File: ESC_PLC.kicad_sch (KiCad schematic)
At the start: 2 parts, among them U2 STM32WBA55HGFx

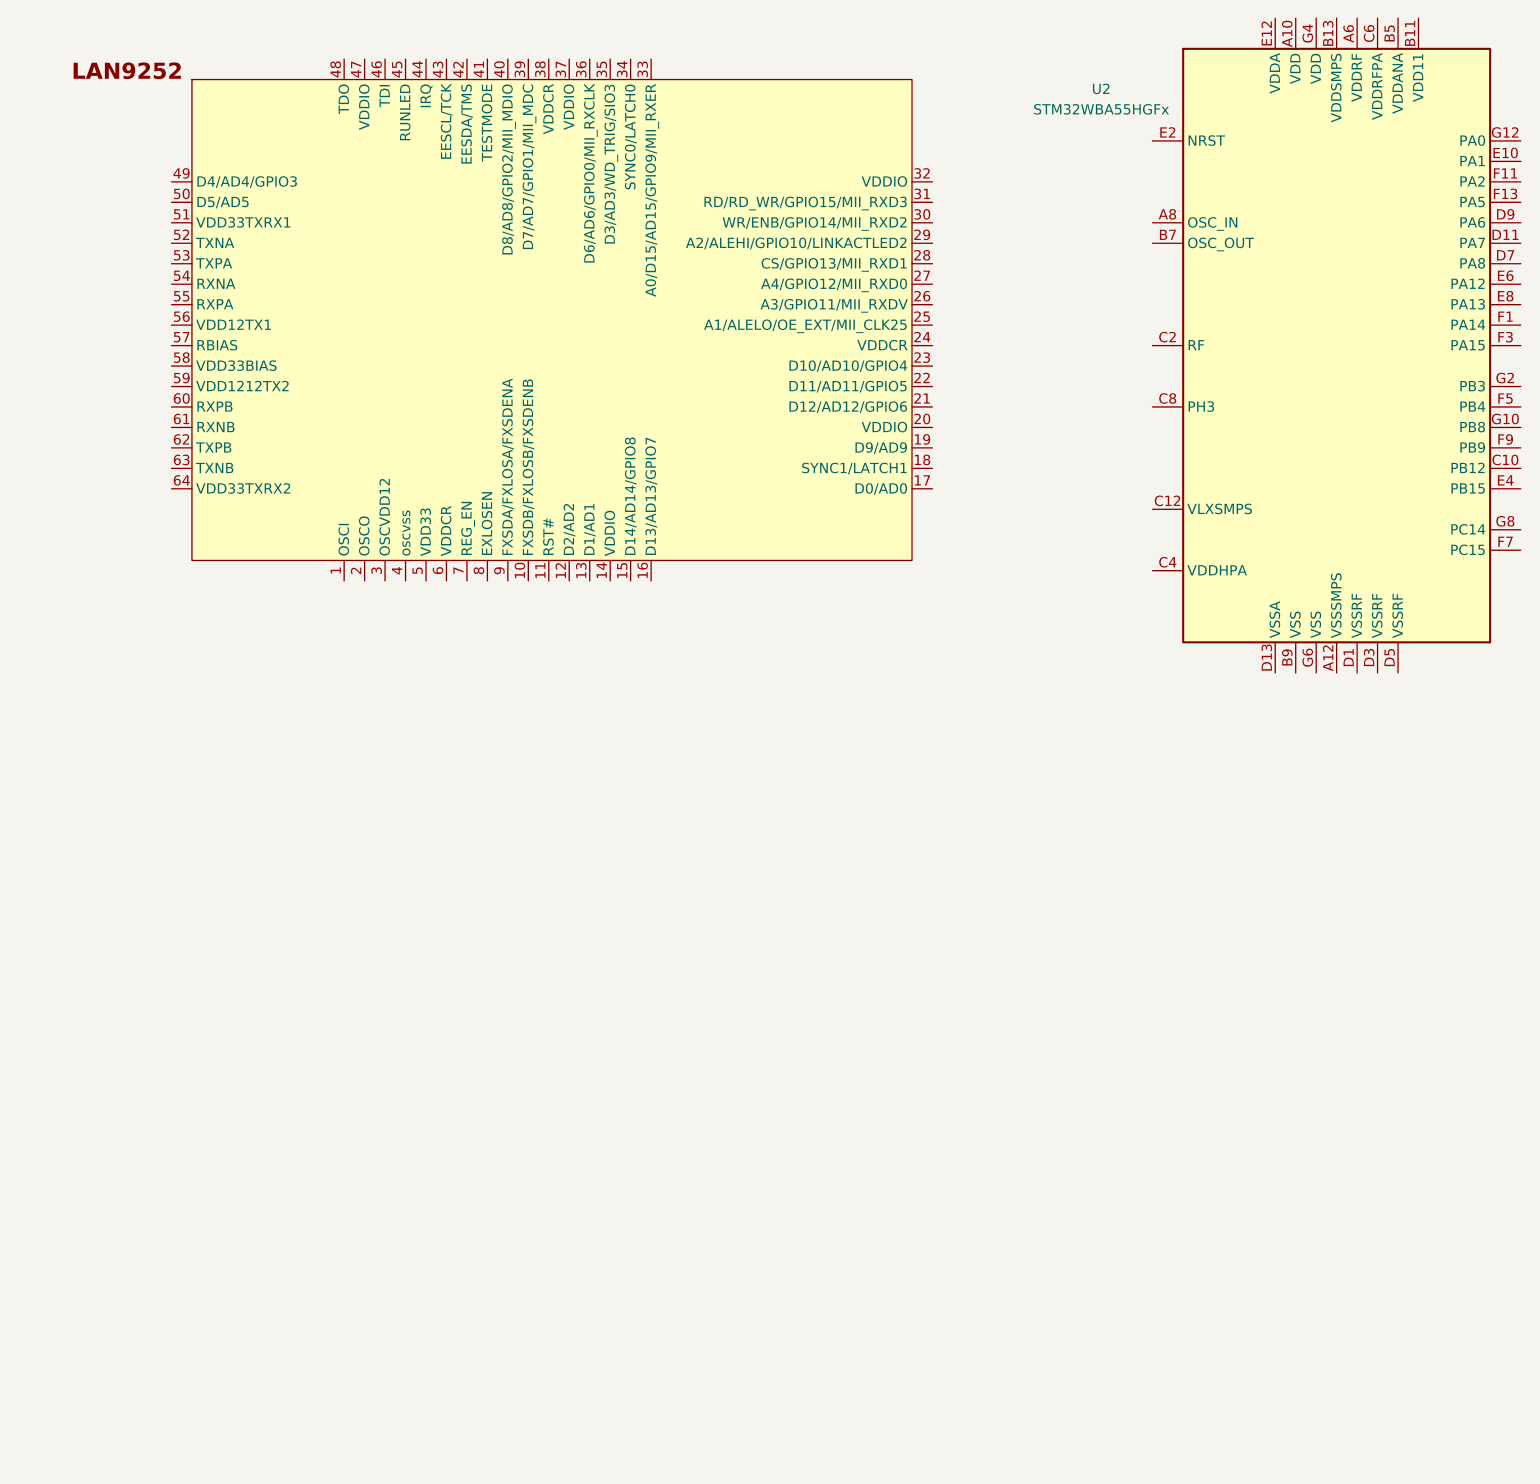
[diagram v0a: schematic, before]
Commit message: Kicad project met ethercat en al paar custom symbolen
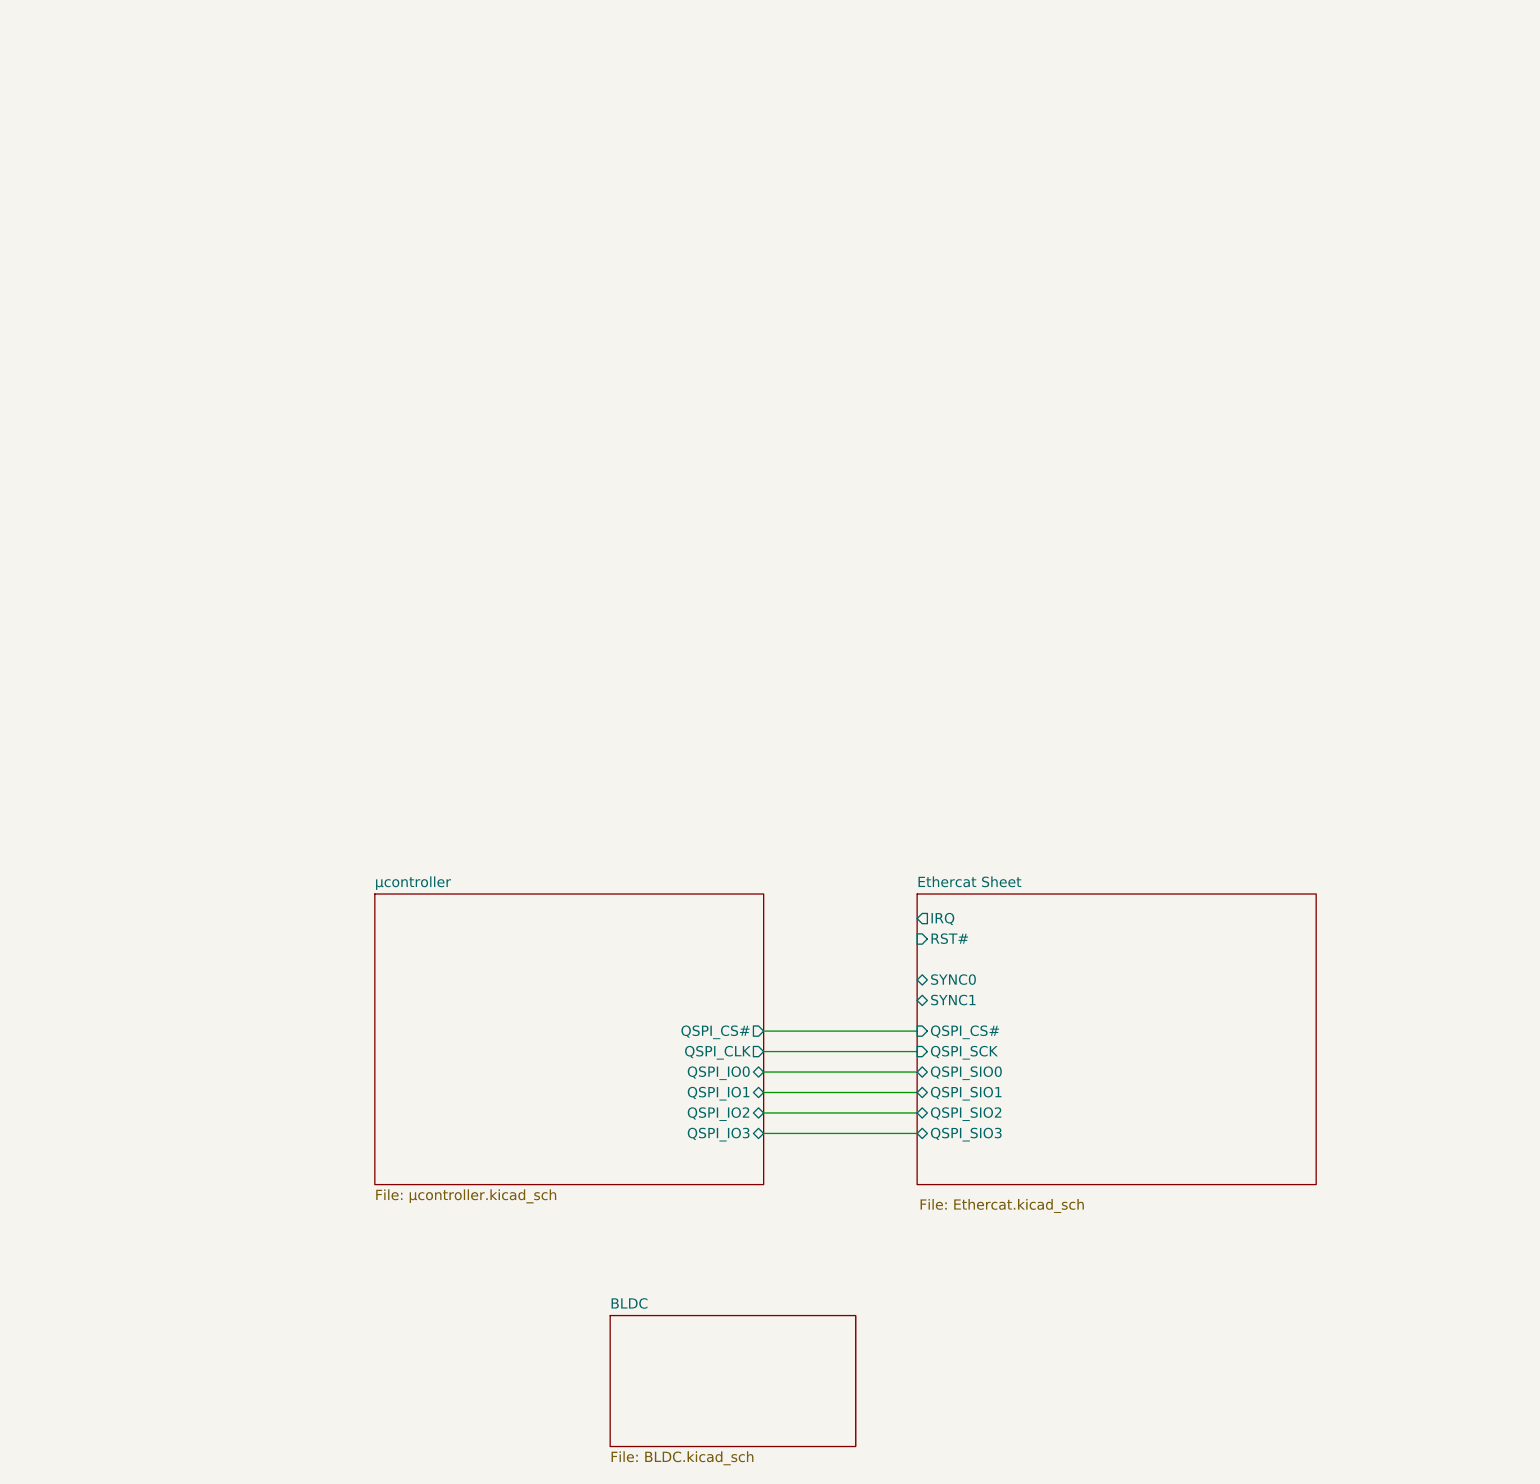
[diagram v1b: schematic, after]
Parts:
- removed U1: (no value), Package_QFP:LQFP-100_14x14mm_P0.5mm, symbol Ethercat:LAN9252
- removed U2: STM32WBA55HGFx, Package_CSP:ST_WLCSP-41_2.98x2.76mm_Layout13x7_P0.4mm_Stagger, symbol MCU_ST_STM32WB:STM32WBA55HGFx
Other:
- added sheet BLDC (BLDC.kicad_sch)
- added sheet Ethercat Sheet (Ethercat.kicad_sch)
- added sheet µcontroller (µcontroller.kicad_sch)

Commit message: Can aangesloten
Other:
- added sheet CAN (CAN.kicad_sch)
- sheet µcontroller ports: added CAN_RX, CAN_SHDN, CAN_STB, CAN_TX; removed none
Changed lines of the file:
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@@
+	(wire
+		(pts
+			(xy 82.55 168.91) (xy 87.63 168.91)
+		)
+		(stroke
+			(width 0)
+			(type default)
+		)
+	)
 	(wire
 		(pts
@@
 	(wire
 		(pts
+			(xy 82.55 166.37) (xy 87.63 166.37)
+		)
+		(stroke
+			(width 0)
+			(type default)
+		)
+	)
+	(wire
+		(pts
+			(xy 82.55 171.45) (xy 87.63 171.45)
+		)
+		(stroke
+			(width 0)
+			(type default)
+		)
+	)
+	(wire
+		(pts
 			(xy 135.89 165.1) (xy 154.94 165.1)
+		)
+		(stroke
+			(width 0)
+			(type default)
+		)
+	)
+	(wire
+		(pts
+			(xy 82.55 173.99) (xy 87.63 173.99)
 		)
 		(stroke
@@
 			)
 		)
+		(pin "CAN_RX" input
+			(at 87.63 168.91 180)
+			(effects
+				(font
+					(size 1.27 1.27)
+				)
+				(justify left)
+			)
+		)
+		(pin "CAN_TX" output
+			(at 87.63 166.37 180)
+			(effects
+				(font
+					(size 1.27 1.27)
+				)
+				(justify left)
+			)
+		)
+		(pin "CAN_SHDN" output
+			(at 87.63 173.99 180)
+			(effects
+				(font
+					(size 1.27 1.27)
+				)
+				(justify left)
+			)
+		)
+		(pin "CAN_STB" output
+			(at 87.63 171.45 180)
+			(effects
+				(font
+					(size 1.27 1.27)
+				)
+				(justify left)
+			)
+		)
 		(instances
 			(project "ESC_PLC"
@@
 				)
 			)
+		)
+	)
+	(sheet
+		(at 43.18 162.56)
+		(size 39.37 13.97)
+		(exclude_from_sim no)
+		(in_bom yes)
+		(on_board yes)
+		(dnp no)
+		(fields_autoplaced yes)
+		(stroke
+			(width 0.1524)
+			(type solid)
+		)
+		(fill
+			(color 0 0 0 0)
+		)
+		(property "Sheetname" "CAN"
+			(at 43.18 161.8484 0)
+			(show_name no)
+			(do_not_autoplace no)
+			(effects
+				(font
+					(size 1.27 1.27)
+				)
+				(justify left bottom)
+			)
+		)
+		(property "Sheetfile" "CAN.kicad_sch"
+			(at 43.18 177.1146 0)
+			(show_name no)
+			(do_not_autoplace no)
+			(effects
+				(font
+					(size 1.27 1.27)
+				)
+				(justify left top)
+			)
+		)
+		(pin "CAN_RXD" input
+			(at 82.55 166.37 0)
+			(effects
+				(font
+					(size 1.27 1.27)
+				)
+				(justify right)
+			)
+		)
+		(pin "CAN_SHDN" input
+			(at 82.55 173.99 0)
+			(effects
+				(font
+					(size 1.27 1.27)
+				)
+				(justify right)
+			)
+		)
+		(pin "CAN_STB" input
+			(at 82.55 171.45 0)
+			(effects
+				(font
+					(size 1.27 1.27)
+				)
+				(justify right)
+			)
+		)
+		(pin "CAN_TXD" output
+			(at 82.55 168.91 0)
+			(effects
+				(font
+					(size 1.27 1.27)
+				)
+				(justify right)
+			)
+		)
+		(instances
+			(project "ESC_PLC"
+				(path "/5bd3bb6f-fe53-443c-806c-077e2bbb5d14"
+					(page "5")
+				)
+			)

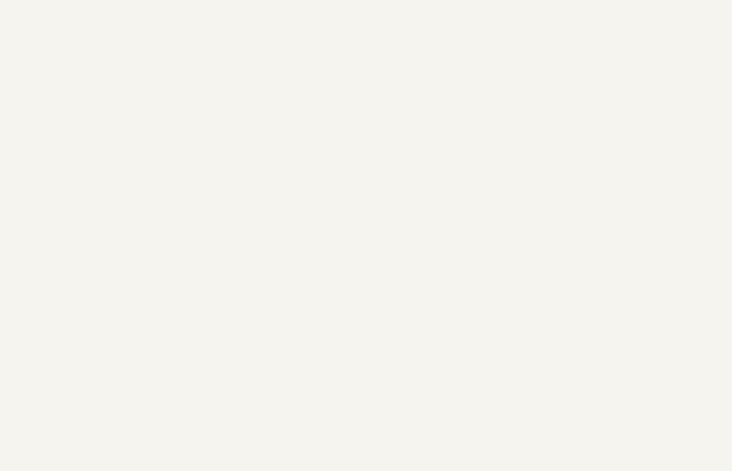
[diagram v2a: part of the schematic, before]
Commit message: power
power ic for 12V->3.3V implemented
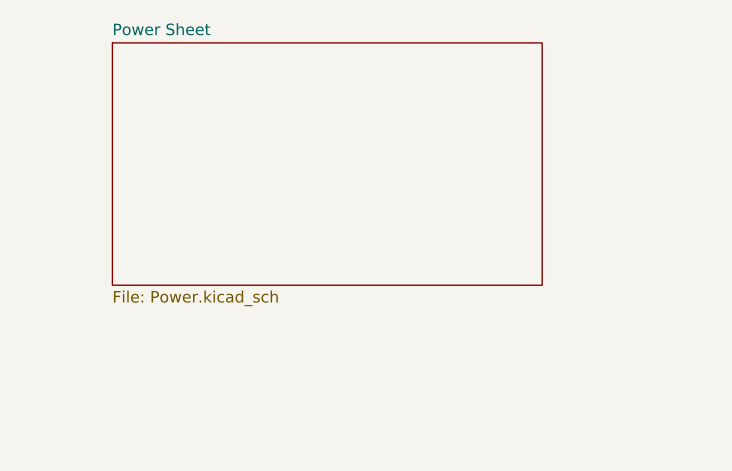
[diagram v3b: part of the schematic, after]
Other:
- added sheet Power Sheet (Power.kicad_sch)
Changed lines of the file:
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@@
+	)
+	(sheet
+		(at 53.594 61.976)
+		(size 47.752 26.924)
+		(exclude_from_sim no)
+		(in_bom yes)
+		(on_board yes)
+		(dnp no)
+		(fields_autoplaced yes)
+		(stroke
+			(width 0.1524)
+			(type solid)
+		)
+		(fill
+			(color 0 0 0 0)
+		)
+		(property "Sheetname" "Power Sheet"
+			(at 53.594 61.2644 0)
+			(show_name no)
+			(do_not_autoplace no)
+			(effects
+				(font
+					(size 1.27 1.27)
+				)
+				(justify left bottom)
+			)
+		)
+		(property "Sheetfile" "Power.kicad_sch"
+			(at 53.594 89.4846 0)
+			(show_name no)
+			(do_not_autoplace no)
+			(effects
+				(font
+					(size 1.27 1.27)
+				)
+				(justify left top)
+			)
+		)
+		(instances
+			(project "ESC_PLC"
+				(path "/5bd3bb6f-fe53-443c-806c-077e2bbb5d14"
+					(page "6")
+				)
+			)
+		)
 	)
 	(sheet
